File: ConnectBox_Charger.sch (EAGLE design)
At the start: 14 parts, among them IC1 M24C32-RDW6TP, J1 CONNECTOR_PI_40_PIN, J2 Lithium Cell, J3 microUSB Power In, J4 FTDI Serial, J5 5V Charger Output, Q1 BSS138, U1 LTC4040

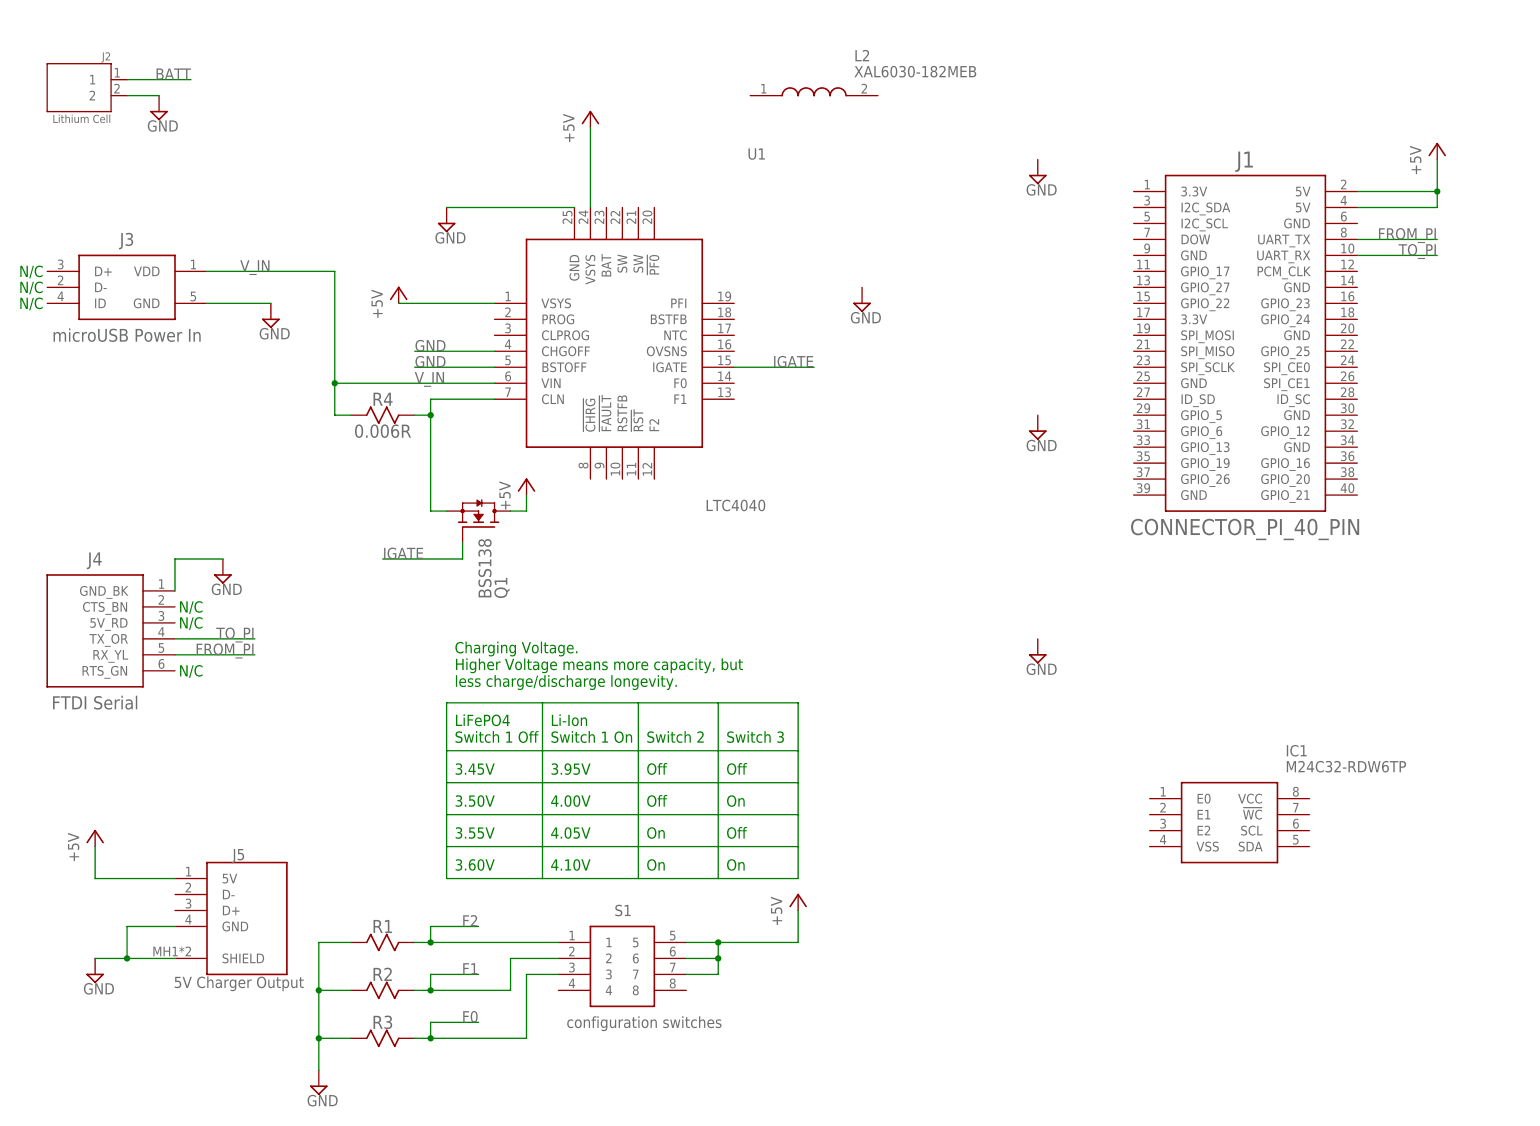
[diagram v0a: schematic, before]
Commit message: almost done just need to connect the SD holder to pins
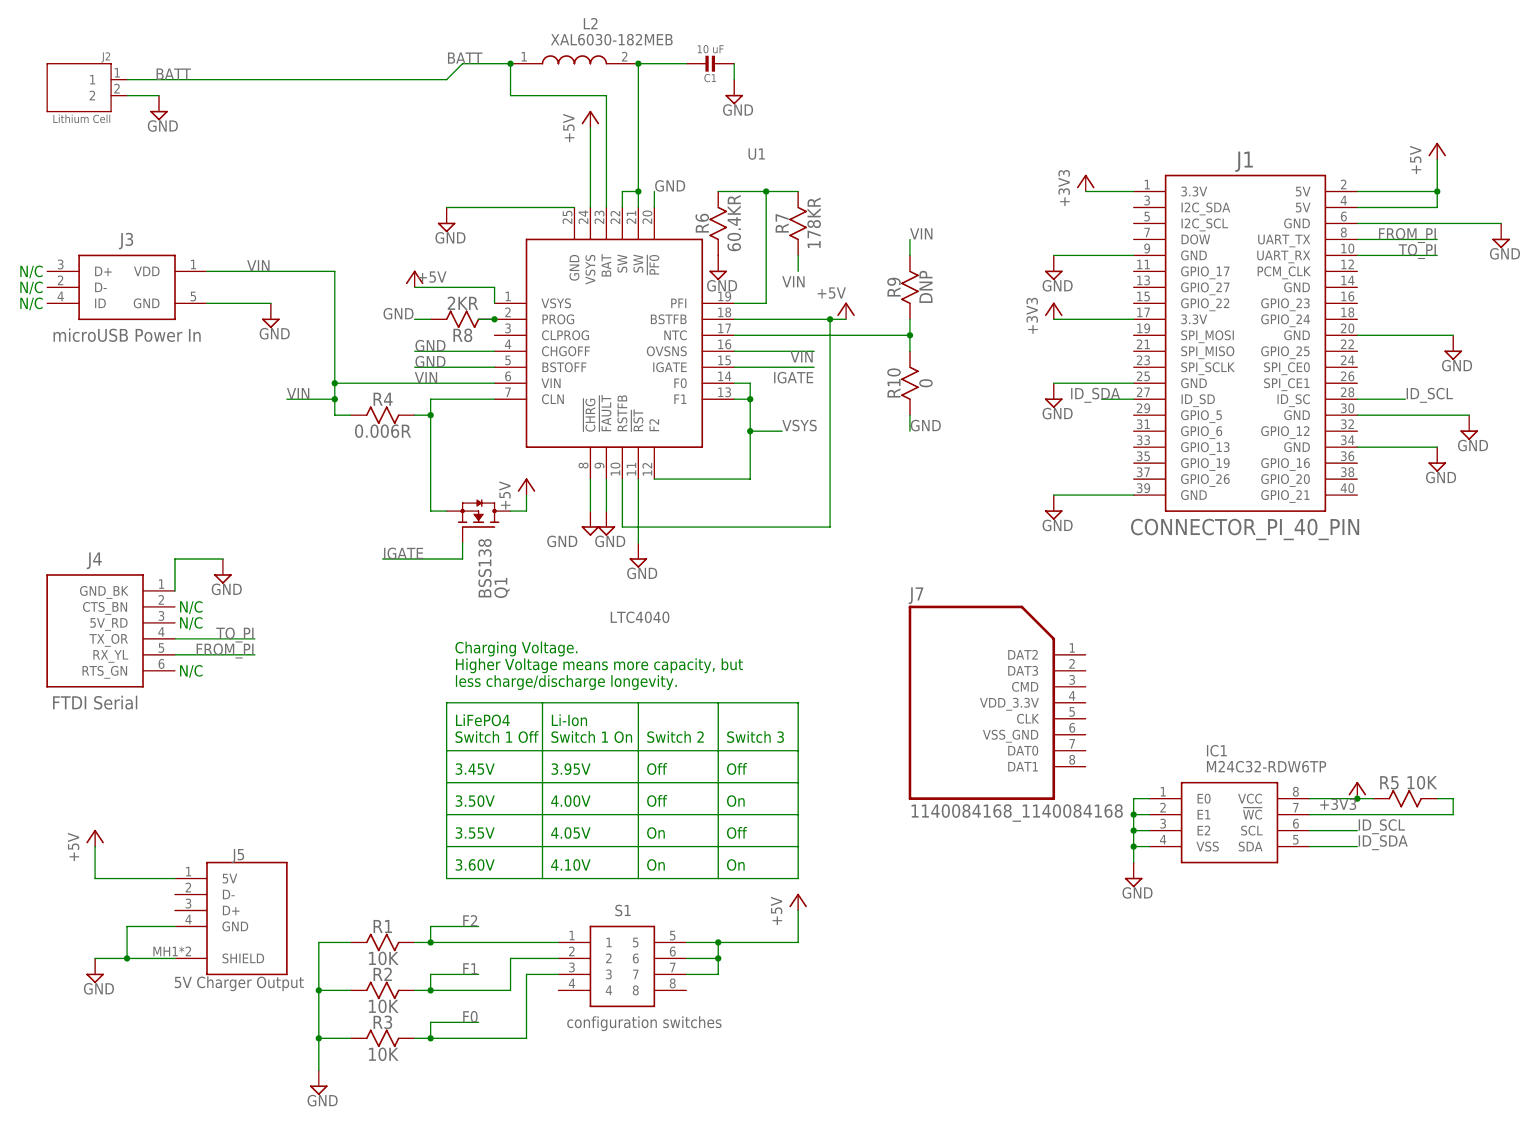
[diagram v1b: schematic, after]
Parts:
- added C1: 10 uF, Adafruit LoRa Radio Bonnet with OLED:MICROBUILDER_CAP_CERAMIC0805_10MGAP
- added J7: 1140084168_1140084168, ConnectBox_2019:1140084168_1140084168
- added R10: 0, ConnectBox_2019:RESISTOR0603
- added R5: 10K, ConnectBox_2019:RESISTOR0603
- added R6: 60.4KR, ConnectBox_2019:RESISTOR0603
- added R7: 178KR, ConnectBox_2019:RESISTOR0603
- added R8: 2KR, ConnectBox_2019:RESISTOR0603
- added R9: DNP, ConnectBox_2019:RESISTOR0603
- R1, R2, R3: value (none) -> 10K
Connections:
- removed net V_IN: J3.VDD, R4.1, U1.VIN@6
- new net +3V3: IC1.VCC, J1.3.3V@1, J1.3.3V@17, R5.2
- new net ID_SCL: IC1.SCL, J1.ID_SC@28
- new net ID_SDA: IC1.SDA, J1.ID_SD@27
- new net N$3: IC1.!WC, R5.1
- new net N$4: R6.2, R7.2, U1.PFI@19
- new net N$5: C1.1, L2.2, U1.SW@21, U1.SW@22
- new net N$6: R8.1, U1.PROG@2
- new net N$9: R10.2, R9.1, U1.NTC@17
- new net VIN: J3.VDD, R4.1, R7.1, R9.2, U1.OVSNS@16, U1.VIN@6
- new net VSYS: U1.F0@14, U1.F1@13, U1.F2@12
- net +5V: now also U1.BSTFB@18, U1.RSTFB@10
- net BATT: now also L2.1, U1.BAT@23
- net GND: now also C1.2, IC1.E0, IC1.E1, IC1.E2, IC1.VSS, J1.GND@20, J1.GND@25, J1.GND@30, J1.GND@34, J1.GND@39, J1.GND@6, J1.GND@9, R10.1, R6.1, R8.2, U1.!CHRG@8, U1.!FAULT@9, U1.!PF0@20, U1.!RST@11
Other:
- moved on the sheet: L2

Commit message: hopefully the last version with the charger
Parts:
- removed J7: 1140084168_1140084168, ConnectBox_2019:1140084168_1140084168
- added J6: 503182-1852, 503182-1852:503182-1852
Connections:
- new net CS: J1.SPI_CE0@24, J6.CD/DAT3
- new net MISO: J1.SPI_MISO@21, J6.DAT0
- new net MOSI: J1.SPI_MOSI@19, J6.CMD
- new net N/C: J6.DAT1, J6.DATA2, J6.DETECT
- new net SCLK: J1.SPI_SCLK@23, J6.CLK
- net +3V3: now also J6.VDD
- net GND: now also J6.SHIELD, J6.VSS

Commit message: Final push ready for ordering as the complete charging accessory for the MAF wifi box project.PCB will connect to RaspPI0W which will distribute wifi and hold essential software.  The PCB will hold content as uploaded and desired by misionaries in the field.
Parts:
- added R11, R14: 49.9K 1%, ConnectBox_2019:RESISTOR0603
- added R12, R13: 75K 1%, ConnectBox_2019:RESISTOR0603
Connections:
- new net N$11: J5.D-@2, R11.1, R12.1
- new net N$8: J5.GND@4, R13.1, R14.1
- net +5V: now also R12.2, R13.2
- net GND: now also R11.2, R14.2; no longer J5.GND@4
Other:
- moved on the sheet: J5, R1, R2, R3, S1
